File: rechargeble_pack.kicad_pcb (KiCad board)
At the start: 2 copper layers, 70 x 33 mm, 42 parts, among them J1 Out, J2 LiPo, J3 DC IN, Q1 IRLML6402, Q2 BC857, Q6 BC847, Q7 BC857, U1 TP4056, U2 TPS61041

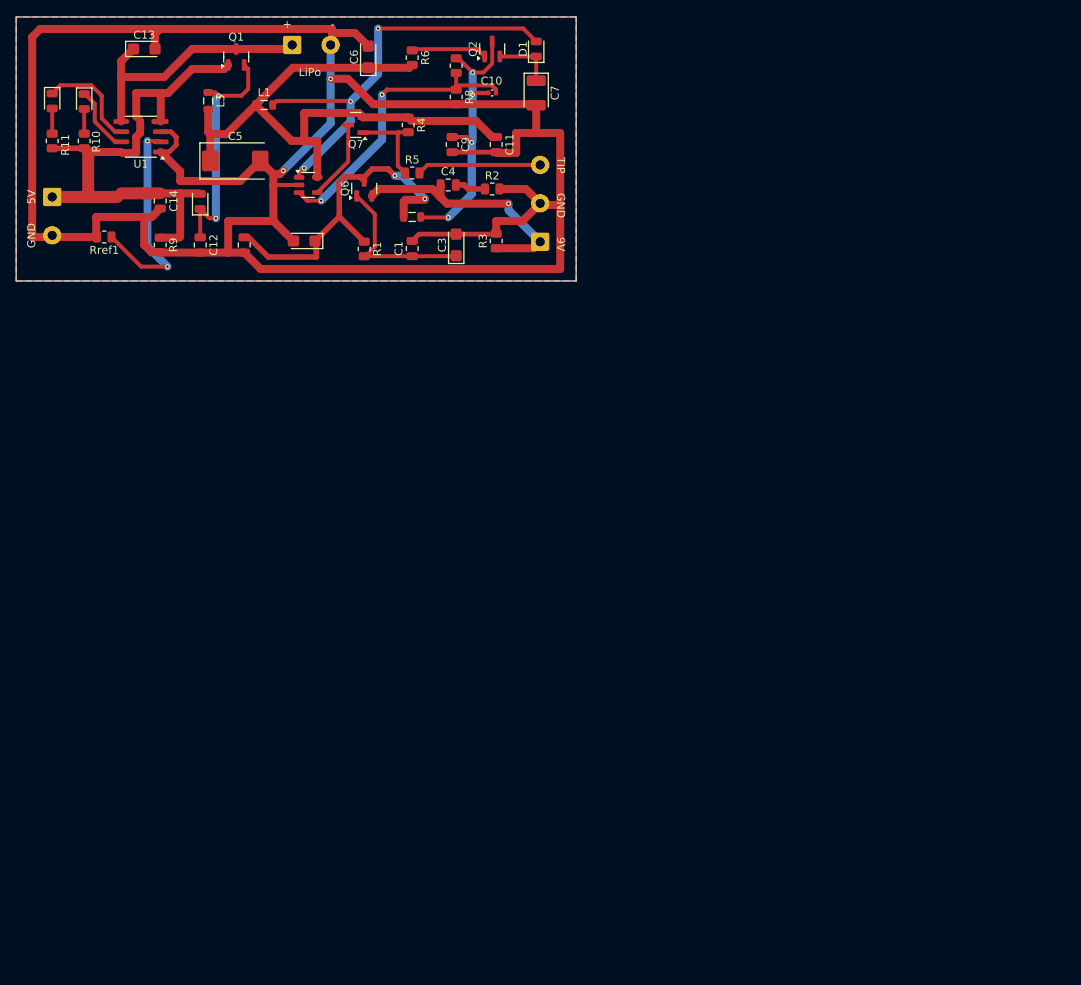
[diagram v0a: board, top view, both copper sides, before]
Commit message: v3 redesign: 31x19 mm one-sided board, regulated 9.0 V, single LED
- Charger TP4057 (500 mA), power-path removed, MLCC instead of tantalum
- Boost TPS61041 at 11.5 V with output disconnect (Q2), EN pull-down fix
- Output chain: RC -> capacitance multiplier -> TPS7A4901 ultra-low-noise LDO, 9.02 V
- Single red/green LED: charging / charged / blinking low-battery (TLV3012)
- USB-C input TVS, project symbol library, JLC basic parts where possible
- New layout 31x19 mm, 2 layers, all SMD on top, ABYSS logo on bottom silk
- production/: gerbers, BOM+CPL for JLCPCB and PCBWay
- README rewritten, .gitignore added, v1 gerbers/BOM/CPL, KiCad backups and caches removed

Co-Authored-By: Claude Opus 5.5 <noreply@anthropic.com>
Claude-Session: https://claude.ai/code/session_01MaiZSNzApBdaqcYQCa8rQi
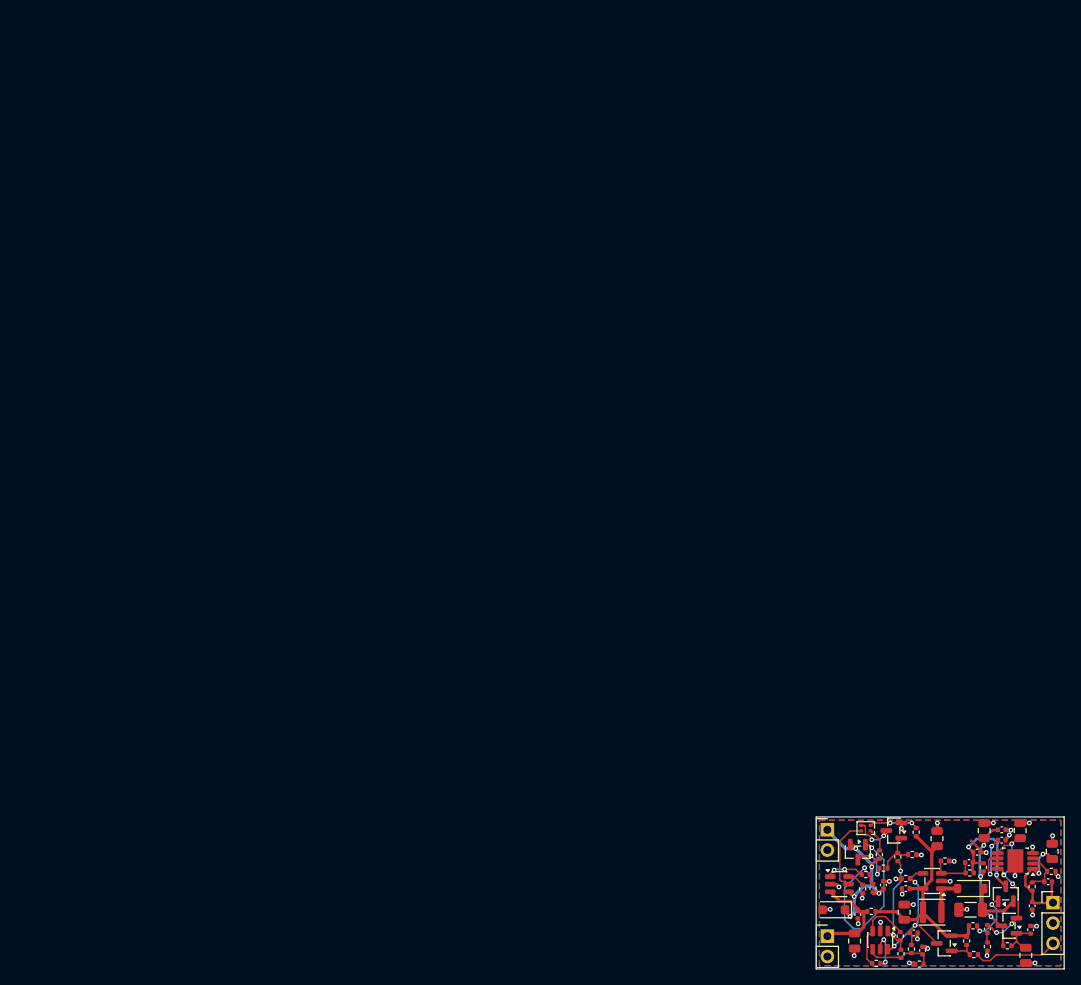
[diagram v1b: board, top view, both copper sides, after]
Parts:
- removed D2: D, Diode_SMD:D_0805_2012Metric
- removed D4: RED, LED_SMD:LED_0805_2012Metric
- removed L2, L3: 10µH, Inductor_SMD:L_0805_2012Metric
- removed Q1: IRLML6402, Package_TO_SOT_SMD:SOT-23
- removed R3: 1M, Resistor_SMD:R_0805_2012Metric
- removed R9: 200k, Resistor_SMD:R_0805_2012Metric
- added C15: 2.2uF 6.3V, Capacitor_SMD:C_0402_1005Metric, F.Cu at (113.3, 116.7)
- added C16: 100nF 16V, Capacitor_SMD:C_0402_1005Metric, F.Cu at (112.2, 114.5)
- added C18: 10uF 25V, Capacitor_SMD:C_0805_2012Metric, F.Cu at (125.5, 101.7)
- added C19: 10uF 25V, Capacitor_SMD:C_0805_2012Metric, F.Cu at (129.5, 104.3)
- added C20: 100nF 50V, Capacitor_SMD:C_0402_1005Metric, F.Cu at (127.0, 111.1)
- added C21: 10nF, Capacitor_SMD:C_0402_1005Metric, F.Cu at (123.2, 102.9)
- added C22: 10nF, Capacitor_SMD:C_0402_1005Metric, F.Cu at (129.0, 108.1)
- added D5: SMF5.0A, Diode_SMD:D_SOD-123F, F.Cu at (102.2, 111.6)
- added Q8: MMBT3904, Package_TO_SOT_SMD:SOT-23, F.Cu at (109.7, 101.7)
- added Q9: S9015, Package_TO_SOT_SMD:SOT-23, F.Cu at (105.2, 104.4)
- added R12: 1M, Resistor_SMD:R_0402_1005Metric, F.Cu at (111.9, 116.5)
- added R13: 10M, Resistor_SMD:R_0402_1005Metric, F.Cu at (112.9, 118.4)
- added R14: 510k, Resistor_SMD:R_0402_1005Metric, F.Cu at (110.6, 117.1)
- added R15: 100k, Resistor_SMD:R_0402_1005Metric, F.Cu at (107.5, 118.3)
- added R16: 1M, Resistor_SMD:R_0402_1005Metric, F.Cu at (110.5, 114.9)
- added R17: 220k, Resistor_SMD:R_0402_1005Metric, F.Cu at (110.2, 105.0)
- added R18: 1M, Resistor_SMD:R_0402_1005Metric, F.Cu at (112.0, 104.7)
- added R19: 100k, Resistor_SMD:R_0402_1005Metric, F.Cu at (106.2, 107.2)
- added R20: 1M, Resistor_SMD:R_0402_1005Metric, F.Cu at (107.1, 108.9)
- added R21: 100k, Resistor_SMD:R_0402_1005Metric, F.Cu at (108.4, 106.4)
- added R22: 1M, Resistor_SMD:R_0402_1005Metric, F.Cu at (111.2, 107.7)
- added R23: 47R, Resistor_SMD:R_0402_1005Metric, F.Cu at (120.9, 106.3)
- added R25: 1R, Resistor_SMD:R_0402_1005Metric, F.Cu at (106.9, 111.8)
- added R26: 330k, Resistor_SMD:R_0402_1005Metric, F.Cu at (127.0, 108.7)
- added R27: 49.9k, Resistor_SMD:R_0402_1005Metric, F.Cu at (129.4, 106.8)
- added U3: TLV3012, Package_TO_SOT_SMD:SOT-23-6, F.Cu at (108.0, 115.4)
- added U4: TPS7A4901DGNR, Package_SO:Texas_DGN0008D_VSSOP-8-1EP_3x3mm_P0.65mm_EP2x2.94mm_Mask1.57x1.89mm, F.Cu at (124.9, 105.5)
- C1, C4, C8, C9: value 100nF -> 100nF 50V; footprint Capacitor_SMD:C_0805_2012Metric -> Capacitor_SMD:C_0402_1005Metric
- C11, C12, C14: value 100nF -> 100nF 16V; footprint Capacitor_SMD:C_0805_2012Metric -> Capacitor_SMD:C_0402_1005Metric
- C13, C6: value 10uF -> 10uF 25V; footprint Capacitor_Tantalum_SMD:CP_EIA-3216-10_Kemet-I -> Capacitor_SMD:C_0805_2012Metric
- C2, C3: value 10uF -> 10uF 50V; footprint Capacitor_Tantalum_SMD:CP_EIA-3216-10_Kemet-I -> Capacitor_SMD:C_0805_2012Metric
- C5: value 100uF -> 22uF 25V; footprint Capacitor_Tantalum_SMD:CP_EIA-7343-15_Kemet-W -> Capacitor_SMD:C_0805_2012Metric
- C7: value 47uF -> 22uF 25V; footprint Capacitor_Tantalum_SMD:CP_EIA-3528-12_Kemet-T -> Capacitor_SMD:C_1206_3216Metric
- D1: value D -> B5819W; footprint Diode_SMD:D_0805_2012Metric -> Diode_SMD:D_SOD-123
- D3: value GREEN -> LTST-C295KGKRKT; footprint LED_SMD:LED_0805_2012Metric -> LED_SMD:LED_LiteOn_LTST-C295K_1.6x0.8mm
- J1: footprint Connector_Wire:SolderWire-0.5sqmm_1x03_P4.8mm_D0.9mm_OD2.3mm -> Connector_PinHeader_2.54mm:PinHeader_1x03_P2.54mm_Vertical
- J2, J3: footprint Connector_Wire:SolderWire-0.5sqmm_1x02_P4.8mm_D0.9mm_OD2.3mm -> Connector_PinHeader_2.54mm:PinHeader_1x02_P2.54mm_Vertical
- L1: value 10µH -> 10uH SWPA3015S100MT; footprint Inductor_SMD:L_0805_2012Metric -> Inductor_SMD:L_Sunlord_SWPA3015S
- Q2, Q7: value BC857 -> S9015
- Q6: value BC847 -> MMBT3904
- R1, R2: footprint Resistor_SMD:R_0805_2012Metric -> Resistor_SMD:R_0402_1005Metric
- R10: value 470R -> 1k; footprint Resistor_SMD:R_0805_2012Metric -> Resistor_SMD:R_0402_1005Metric
- R11: value 270R -> 1k; footprint Resistor_SMD:R_0805_2012Metric -> Resistor_SMD:R_0402_1005Metric
- R4: value 47k -> 1M; footprint Resistor_SMD:R_0805_2012Metric -> Resistor_SMD:R_0402_1005Metric
- R5: value 47k -> 470k; footprint Resistor_SMD:R_0805_2012Metric -> Resistor_SMD:R_0402_1005Metric
- R6: value 47k -> 330k; footprint Resistor_SMD:R_0805_2012Metric -> Resistor_SMD:R_0402_1005Metric
- R7: value 1M43 -> 1M; footprint Resistor_SMD:R_0805_2012Metric -> Resistor_SMD:R_0402_1005Metric
- R8: value 200k -> 120k; footprint Resistor_SMD:R_0805_2012Metric -> Resistor_SMD:R_0402_1005Metric
- Rref1: value 1.58K -> 2k; footprint Resistor_SMD:R_0805_2012Metric -> Resistor_SMD:R_0402_1005Metric
- U1: value TP4056 -> TP4057; footprint Package_SO:SOIC-8_3.9x4.9mm_P1.27mm -> Package_TO_SOT_SMD:SOT-23-6
- moved C13 142.5 mm to (104.8, 115.5), turned to -90 degrees
- moved R11 136.6 mm to (107.9, 104.7)
- moved D3 136.4 mm to (106.2, 101.4), turned to 180 degrees
- moved R10 135.2 mm to (112.5, 101.9)
- moved L1 131.0 mm to (114.5, 111.9)
- moved J2 129.9 mm to (101.4, 114.9)
- moved R6 129.2 mm to (119.6, 113.6), turned to 180 degrees
- moved U1 127.9 mm to (102.9, 108.4), turned to 0 degrees
- moved Q7 126.0 mm to (116.0, 115.8)
- moved C5 125.7 mm to (111.0, 111.9), turned to 90 degrees
- moved J3 125.1 mm to (101.4, 101.6), turned to 0 degrees
- moved Rref1 125.0 mm to (105.8, 109.0), turned to -90 degrees
- moved C14 124.4 mm to (108.4, 108.5), turned to 90 degrees
- moved R4 123.6 mm to (118.8, 115.5)
- moved Q2 123.6 mm to (123.7, 109.6)
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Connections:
- net /OUT_EN renamed OUT_EN
- net Net-(Q7-C) renamed VSW
- C12 pad 1: Net-(D2-K) -> +BATT
- C4 pad 1: +9V -> PRE9
- D3 pad 1: Net-(D3-K) -> Net-(R11-Pad1)
- D3 pad 2: Net-(D3-A) -> Net-(R10-Pad1)
- Q6 pad 2: +9V -> PRE9
- R10 pad 1: Net-(D4-A) -> Net-(R10-Pad1)
- R10 pad 2: VBUS -> VCC
- R11 pad 1: Net-(D3-A) -> Net-(R11-Pad1)
- Rref1 pad 1: Net-(U1-PROG) -> Net-(Rref1-Pad1)
- U1 pad 1: GND -> CHRG_N
- U1 pad 2: Net-(U1-PROG) -> GND
- U1 pad 3: GND -> +BATT
- U1 pad 5: +BATT -> Net-(D3-Pad3)
- U1 pad 6: Net-(D3-K) -> Net-(Rref1-Pad1)
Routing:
- net GND: track 305.9 -> 30.5 mm, vias 2 -> 32
- net VCC: track 78.3 -> 28.3 mm
- net Net-(U2-Pad1): track 54.0 -> 4.95 mm, vias 3 -> 0
- net VBUS: track 68.9 -> 23.1 mm, vias 0 -> 5
- net Net-(R7-Pad2): track 38.6 -> 5.96 mm, vias 2 -> 0
- net Net-(D2-K): track 30.2 -> 0.00 mm, vias 2 -> 0
- net Net-(U1-PROG): track 27.0 -> 0.00 mm, vias 2 -> 0
- net +10V: track 44.2 -> 17.9 mm, vias 2 -> 3
- net Q9_B: track 0.00 -> 25.4 mm, vias 0 -> 2
- net Net-(R7-Pad1): track 36.1 -> 15.3 mm, vias 4 -> 2
- net +BATT: track 33.4 -> 12.7 mm
- net PRE9: track 0.00 -> 20.4 mm, vias 0 -> 5
- net +9V: track 31.9 -> 15.6 mm, vias 1 -> 2
- net Net-(C1-Pad1): track 20.6 -> 5.15 mm
- net Net-(D3-K): track 13.1 -> 0.00 mm
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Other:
- board size 70 x 33 mm -> 31 x 19 mm
- board text added: "+9V"
- board text added: "5V IN"
- board text added: "BAT+"
- board text added: "RING"
- board text removed: "+"
- board text removed: "-"
- board text removed: "5V"
- board text removed: "9V"
- board text removed: "LiPo"
- board text removed: "TIP"
